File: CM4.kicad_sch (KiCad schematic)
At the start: 11 parts, among them J11 Conn_02x05_Odd_Even, J13 Conn_01x02, J14 Conn_01x02, J15 Conn_01x02, J6 HDMI_A_2.0, U1 RaspberryPi-CM4Lite, U100 DF40C-100DS-0.4V(51), U101 DF40C-100DS-0.4V(51)

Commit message: Adjust Manufacturer/PartNumber for some parts
- Use Diodes B2100-13-F consistently
- Define part for pin headers
- Replace N-Channel MOSFET for PoE with BSZ440N10NS3GATMA1
- Define Input protection MOSFET DMP3013SFV-7

Signed-off-by: Stefan Agner <stefan@agner.ch>
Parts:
- J13, J14, J15: Manufacturer (none) -> Adam Tech; PartNumber (none) -> PH1-02-UA
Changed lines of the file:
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@@
     (comment 2 "Light Blue")
   )
+  (bus_alias "PCIe" (members "~RST" "~CLKREQ" "CLK+" "CLK-" "TX+" "TX-" "RX+" "RX-"))
+  (bus_alias "SD" (members "D[0..3]" "CMD" "CLK" "PWR" "DET"))
+  (bus_alias "HDMI" (members "D0+" "D0-" "D1+" "D1-" "D2+" "D2-" "CLK+" "CLK-" "CEC" "HPD" "SDA" "SCL"))
   (bus_alias "UART" (members "TXD" "RXD" "CTS" "RTS"))
-  (bus_alias "HDMI" (members "D0+" "D0-" "D1+" "D1-" "D2+" "D2-" "CLK+" "CLK-" "CEC" "HPD" "SDA" "SCL"))
-  (bus_alias "SD" (members "D[0..3]" "CMD" "CLK" "PWR" "DET"))
-  (bus_alias "PCIe" (members "~RST" "~CLKREQ" "CLK+" "CLK-" "TX+" "TX-" "RX+" "RX-"))
   (junction (at 59.055 173.99) (diameter 0.9144) (color 0 0 0 0))
   (junction (at 121.92 171.45) (diameter 0.9144) (color 0 0 0 0))
@@
       (effects (font (size 1.27 1.27)) hide)
     )
+    (property "Manufacturer" "Adam Tech" (id 4) (at 133.985 157.48 0)
+      (effects (font (size 1.27 1.27)) hide)
+    )
+    (property "PartNumber" "PH1-02-UA" (id 5) (at 133.985 157.48 0)
+      (effects (font (size 1.27 1.27)) hide)
+    )
     (pin "1")
     (pin "2")
@@
     )
     (property "Config" "DNP" (id 4) (at 139.065 174.625 0))
+    (property "Manufacturer" "Adam Tech" (id 5) (at 133.985 171.45 0)
+      (effects (font (size 1.27 1.27)) hide)
+    )
+    (property "PartNumber" "PH1-02-UA" (id 6) (at 133.985 171.45 0)
+      (effects (font (size 1.27 1.27)) hide)
+    )
     (pin "1")
     (pin "2")
@@
     )
     (property "Config" "DNP" (id 4) (at 139.065 186.69 0))
+    (property "Manufacturer" "Adam Tech" (id 5) (at 133.985 182.88 0)
+      (effects (font (size 1.27 1.27)) hide)
+    )
+    (property "PartNumber" "PH1-02-UA" (id 6) (at 133.985 182.88 0)
+      (effects (font (size 1.27 1.27)) hide)
+    )
     (pin "1")
     (pin "2")

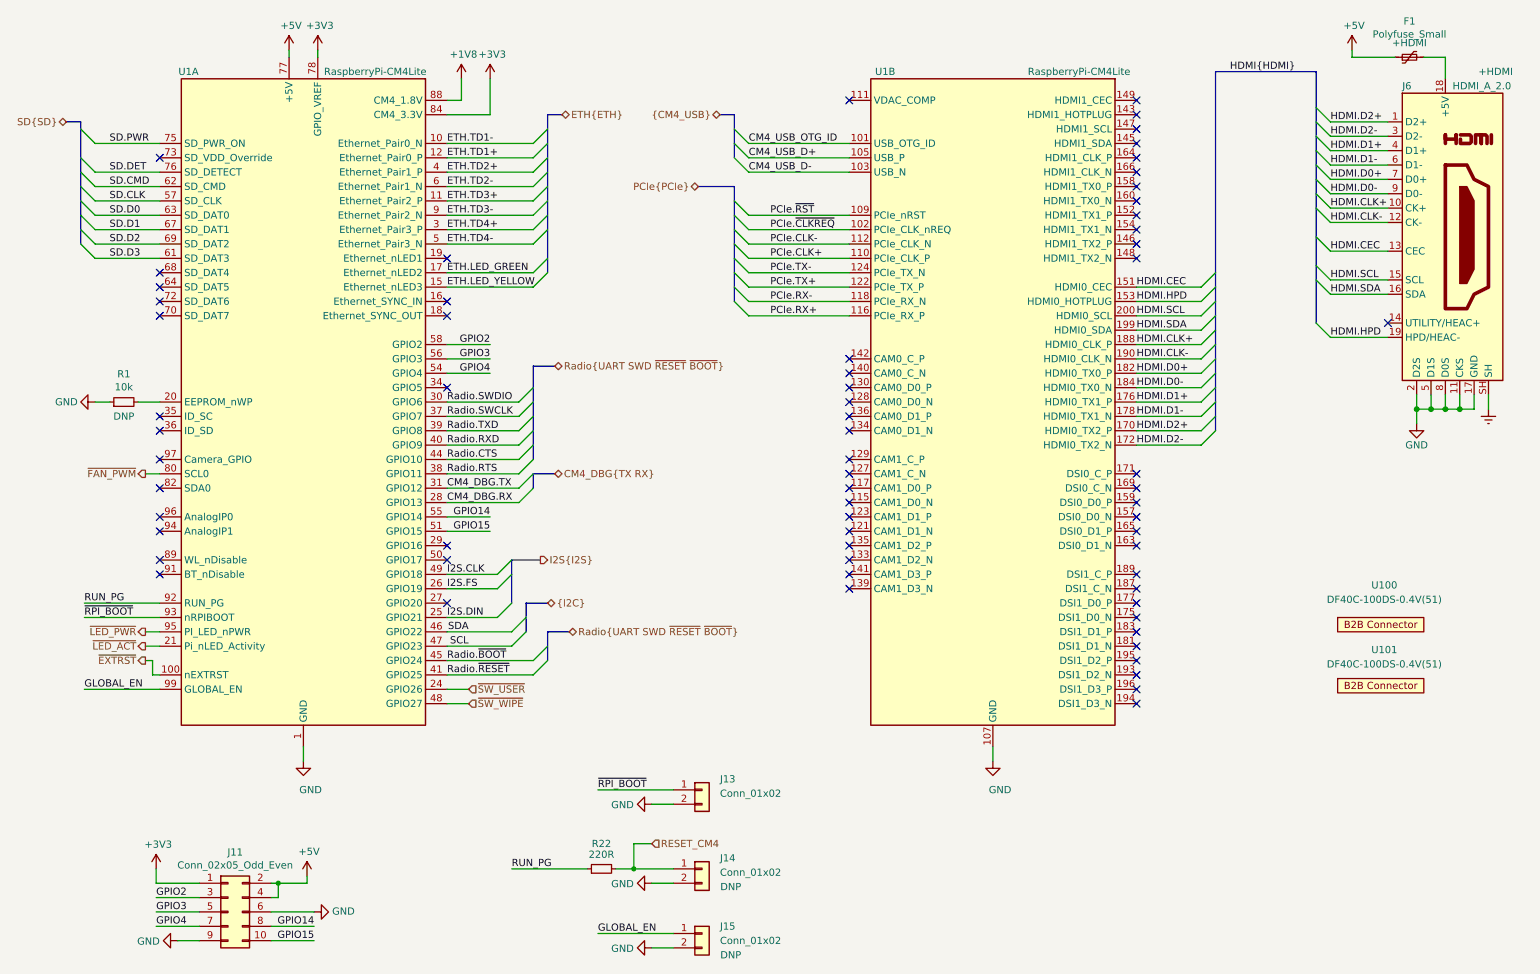
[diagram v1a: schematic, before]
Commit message: Reannotate the complete schematics
Signed-off-by: Stefan Agner <stefan@agner.ch>
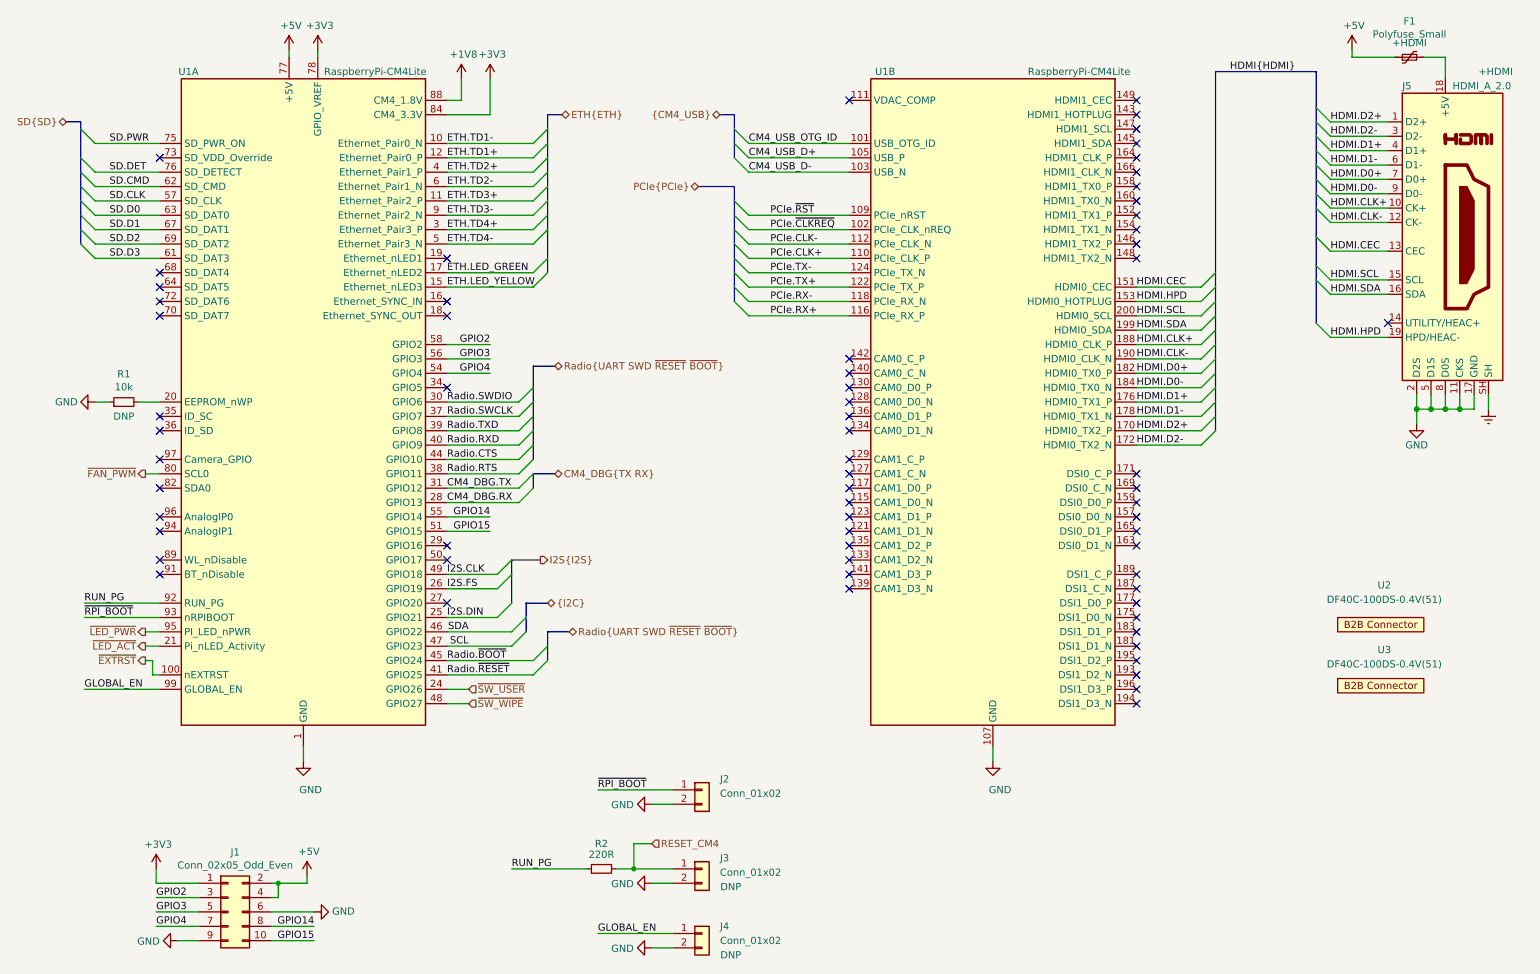
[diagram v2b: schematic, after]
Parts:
- renumbered J11 to J1, J13 to J2, J14 to J3, J15 to J4, J6 to J5, R22 to R2, U100 to U2, U101 to U3
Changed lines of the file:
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@@
   (symbol (lib_id "power:+3V3") (at 37.465 171.45 0) (unit 1)
     (in_bom yes) (on_board yes)
-    (property "Reference" "#PWR0111" (id 0) (at 37.465 175.26 0)
+    (property "Reference" "#PWR02" (id 0) (at 37.465 175.26 0)
       (effects (font (size 1.27 1.27)) hide)
     )
@@
   (symbol (lib_id "power:+5V") (at 60.96 26.67 0) (unit 1)
     (in_bom yes) (on_board yes)
-    (property "Reference" "#PWR0105" (id 0) (at 60.96 30.48 0)
+    (property "Reference" "#PWR04" (id 0) (at 60.96 30.48 0)
       (effects (font (size 1.27 1.27)) hide)
     )
@@
   (symbol (lib_id "power:+5V") (at 64.135 172.72 0) (unit 1)
     (in_bom yes) (on_board yes)
-    (property "Reference" "#PWR0112" (id 0) (at 64.135 176.53 0)
+    (property "Reference" "#PWR06" (id 0) (at 64.135 176.53 0)
       (effects (font (size 1.27 1.27)) hide)
     )
@@
   (symbol (lib_id "power:+3V3") (at 66.04 26.67 0) (unit 1)
     (in_bom yes) (on_board yes)
-    (property "Reference" "#PWR0106" (id 0) (at 66.04 30.48 0)
+    (property "Reference" "#PWR08" (id 0) (at 66.04 30.48 0)
       (effects (font (size 1.27 1.27)) hide)
     )
@@
   (symbol (lib_id "power:+1V8") (at 91.44 31.75 0) (unit 1)
     (in_bom yes) (on_board yes)
-    (property "Reference" "#PWR0107" (id 0) (at 91.44 35.56 0)
+    (property "Reference" "#PWR09" (id 0) (at 91.44 35.56 0)
       (effects (font (size 1.27 1.27)) hide)
     )
@@
   (symbol (lib_id "power:+3V3") (at 96.52 31.75 0) (unit 1)
     (in_bom yes) (on_board yes)
-    (property "Reference" "#PWR0108" (id 0) (at 96.52 35.56 0)
+    (property "Reference" "#PWR010" (id 0) (at 96.52 35.56 0)
       (effects (font (size 1.27 1.27)) hide)
     )
@@
   (symbol (lib_id "power:+5V") (at 248.92 26.67 0) (unit 1)
     (in_bom yes) (on_board yes)
-    (property "Reference" "#PWR0103" (id 0) (at 248.92 30.48 0)
+    (property "Reference" "#PWR015" (id 0) (at 248.92 30.48 0)
       (effects (font (size 1.27 1.27)) hide)
     )
@@
   (symbol (lib_id "power:GND") (at 26.67 88.9 270) (unit 1)
     (in_bom yes) (on_board yes)
-    (property "Reference" "#PWR0104" (id 0) (at 20.32 88.9 0)
+    (property "Reference" "#PWR01" (id 0) (at 20.32 88.9 0)
       (effects (font (size 1.27 1.27)) hide)
     )
@@
   (symbol (lib_id "power:GND") (at 41.275 184.15 270) (unit 1)
     (in_bom yes) (on_board yes)
-    (property "Reference" "#PWR0110" (id 0) (at 34.925 184.15 0)
+    (property "Reference" "#PWR03" (id 0) (at 34.925 184.15 0)
       (effects (font (size 1.27 1.27)) hide)
     )
@@
   (symbol (lib_id "power:GND") (at 63.5 152.4 0) (unit 1)
     (in_bom yes) (on_board yes)
-    (property "Reference" "#PWR0109" (id 0) (at 63.5 158.75 0)
+    (property "Reference" "#PWR05" (id 0) (at 63.5 158.75 0)
       (effects (font (size 1.27 1.27)) hide)
     )
@@
   (symbol (lib_id "power:GND") (at 65.405 179.07 90) (unit 1)
     (in_bom yes) (on_board yes)
-    (property "Reference" "#PWR0113" (id 0) (at 71.755 179.07 0)
+    (property "Reference" "#PWR07" (id 0) (at 71.755 179.07 0)
       (effects (font (size 1.27 1.27)) hide)
     )
@@
   (symbol (lib_id "power:GND") (at 125.095 160.02 270) (unit 1)
     (in_bom yes) (on_board yes)
-    (property "Reference" "#PWR0190" (id 0) (at 118.745 160.02 0)
+    (property "Reference" "#PWR011" (id 0) (at 118.745 160.02 0)
       (effects (font (size 1.27 1.27)) hide)
     )
@@
   (symbol (lib_id "power:GND") (at 125.095 173.99 270) (unit 1)
     (in_bom yes) (on_board yes)
-    (property "Reference" "#PWR0127" (id 0) (at 118.745 173.99 0)
+    (property "Reference" "#PWR012" (id 0) (at 118.745 173.99 0)
       (effects (font (size 1.27 1.27)) hide)
     )
@@
   (symbol (lib_id "power:GND") (at 125.095 185.42 270) (unit 1)
     (in_bom yes) (on_board yes)
-    (property "Reference" "#PWR0125" (id 0) (at 118.745 185.42 0)
+    (property "Reference" "#PWR013" (id 0) (at 118.745 185.42 0)
       (effects (font (size 1.27 1.27)) hide)
     )
@@
   (symbol (lib_id "power:GND") (at 185.42 152.4 0) (unit 1)
     (in_bom yes) (on_board yes)
-    (property "Reference" "#PWR0114" (id 0) (at 185.42 158.75 0)
+    (property "Reference" "#PWR014" (id 0) (at 185.42 158.75 0)
       (effects (font (size 1.27 1.27)) hide)
     )
@@
   (symbol (lib_id "power:GND") (at 260.35 92.71 0) (unit 1)
     (in_bom yes) (on_board yes)
-    (property "Reference" "#PWR0101" (id 0) (at 260.35 99.06 0)
+    (property "Reference" "#PWR016" (id 0) (at 260.35 99.06 0)
       (effects (font (size 1.27 1.27)) hide)
     )
@@
   (symbol (lib_id "power:Earth") (at 273.05 90.17 0) (unit 1)
     (in_bom yes) (on_board yes)
-    (property "Reference" "#PWR0102" (id 0) (at 273.05 96.52 0)
+    (property "Reference" "#PWR017" (id 0) (at 273.05 96.52 0)
       (effects (font (size 1.27 1.27)) hide)
     )
@@
   (symbol (lib_id "Device:R_Small") (at 116.205 171.45 90) (unit 1)
     (in_bom yes) (on_board yes)
-    (property "Reference" "R22" (id 0) (at 116.205 167.005 90))
+    (property "Reference" "R2" (id 0) (at 116.205 167.005 90))
     (property "Value" "220R" (id 1) (at 116.205 168.91 90))
     (property "Footprint" "Resistor_SMD:R_0402_1005Metric" (id 2) (at 116.205 171.45 0)
@@
   (symbol (lib_id "Connector_Generic:Conn_01x02") (at 133.985 157.48 0) (unit 1)
     (in_bom yes) (on_board yes)
-    (property "Reference" "J13" (id 0) (at 137.16 155.5749 0)
+    (property "Reference" "J2" (id 0) (at 137.16 155.5749 0)
       (effects (font (size 1.27 1.27)) (justify left))
     )
@@
   (symbol (lib_id "Connector_Generic:Conn_01x02") (at 133.985 171.45 0) (unit 1)
     (in_bom yes) (on_board yes)
-    (property "Reference" "J14" (id 0) (at 137.16 169.5449 0)
+    (property "Reference" "J3" (id 0) (at 137.16 169.5449 0)
       (effects (font (size 1.27 1.27)) (justify left))
     )
@@
   (symbol (lib_id "Connector_Generic:Conn_01x02") (at 133.985 182.88 0) (unit 1)
     (in_bom yes) (on_board yes)
-    (property "Reference" "J15" (id 0) (at 137.16 181.6099 0)
+    (property "Reference" "J4" (id 0) (at 137.16 181.6099 0)
       (effects (font (size 1.27 1.27)) (justify left))
     )
@@
   (symbol (lib_id "LightBlue:DF40C-100DS-0.4V(51)") (at 254 128.27 0) (unit 1)
     (in_bom yes) (on_board no)
-    (property "Reference" "U100" (id 0) (at 254.635 121.285 0))
+    (property "Reference" "U2" (id 0) (at 254.635 121.285 0))
     (property "Value" "DF40C-100DS-0.4V(51)" (id 1) (at 254.635 123.825 0))
     (property "Footprint" "" (id 2) (at 254 128.27 0)
@@
   (symbol (lib_id "LightBlue:DF40C-100DS-0.4V(51)") (at 254 139.065 0) (unit 1)
     (in_bom yes) (on_board no)
-    (property "Reference" "U101" (id 0) (at 254.635 132.715 0))
+    (property "Reference" "U3" (id 0) (at 254.635 132.715 0))
     (property "Value" "DF40C-100DS-0.4V(51)" (id 1) (at 254.635 135.255 0))
     (property "Footprint" "" (id 2) (at 254 139.065 0)
@@
   (symbol (lib_id "Connector_Generic:Conn_02x05_Odd_Even") (at 50.165 179.07 0) (unit 1)
     (in_bom yes) (on_board yes)
-    (property "Reference" "J11" (id 0) (at 51.435 168.5098 0))
+    (property "Reference" "J1" (id 0) (at 51.435 168.5098 0))
     (property "Value" "Conn_02x05_Odd_Even" (id 1) (at 51.435 170.8085 0))
     (property "Footprint" "Connector_PinHeader_2.54mm:PinHeader_2x05_P2.54mm_Vertical" (id 2) (at 50.165 179.07 0)
@@
   (symbol (lib_id "Connector:HDMI_A_1.4") (at 265.43 59.69 0) (unit 1)
     (in_bom yes) (on_board yes)
-    (property "Reference" "J6" (id 0) (at 257.81 33.02 0)
-      (effects (font (size 1.27 1.27)) (justify left))
-    )
+    (property "Reference" "J5" (id 0) (at 257.81 33.02 0)
+      (effects (font (size 1.27 1.27)) (justify left))
+    )

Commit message: Adjust rating/footprint size of some ceramic capacitors
Also update connector/jumper designator to make more sense.

Signed-off-by: Stefan Agner <stefan@agner.ch>
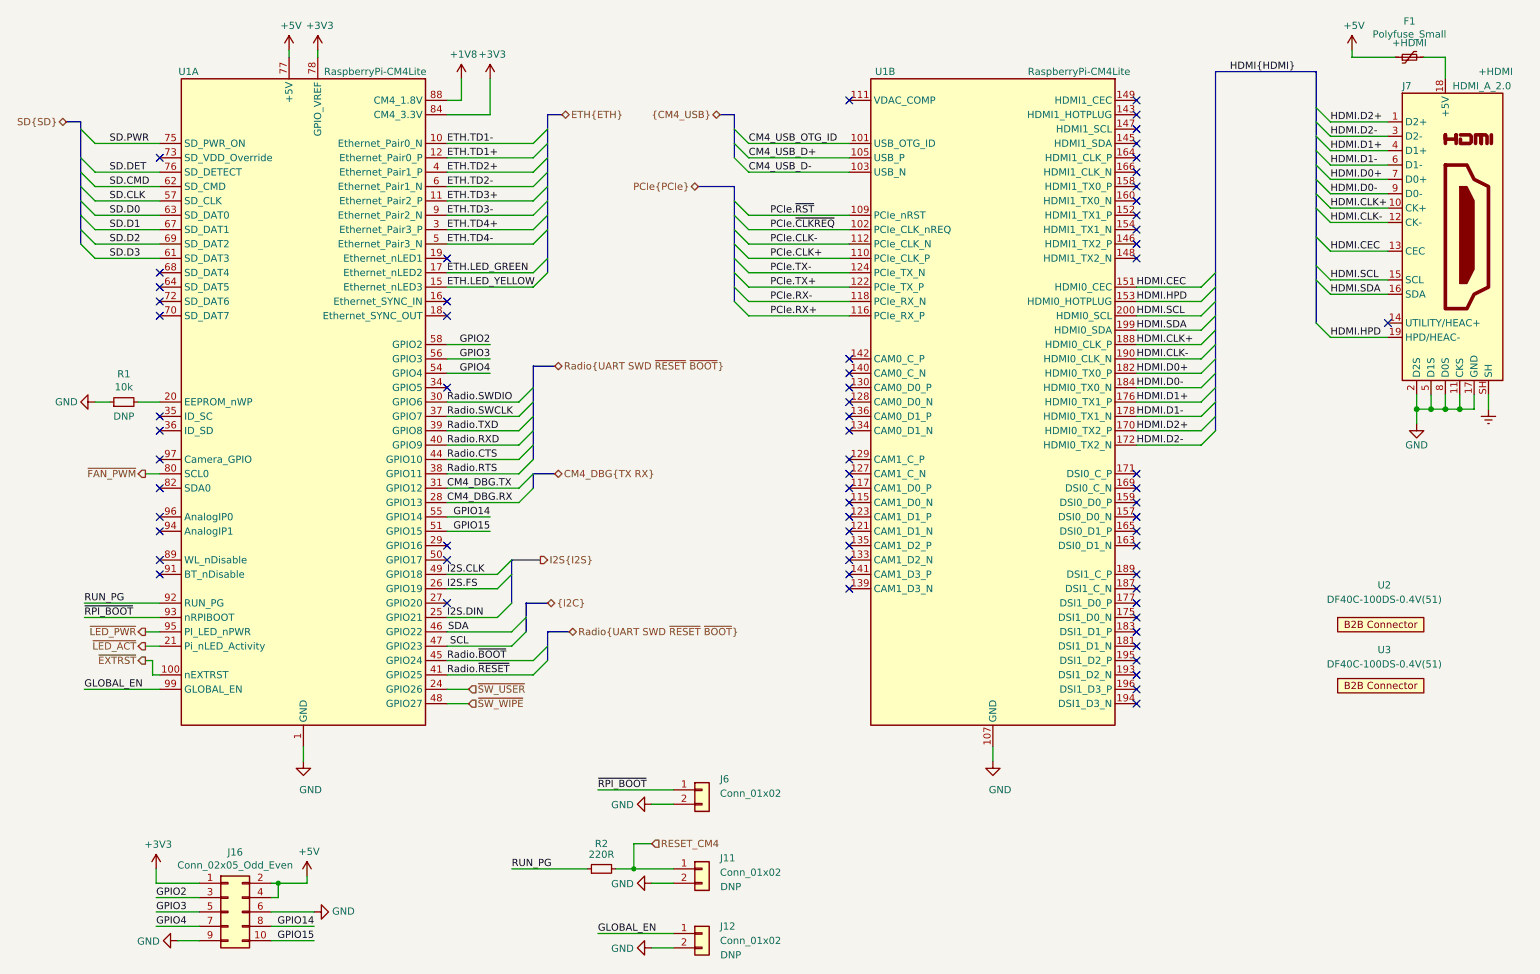
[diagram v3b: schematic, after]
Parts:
- renumbered J3 to J11, J4 to J12, J1 to J16, J2 to J6, J5 to J7
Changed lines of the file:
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@@
   (symbol (lib_id "Connector_Generic:Conn_01x02") (at 133.985 157.48 0) (unit 1)
     (in_bom yes) (on_board yes)
-    (property "Reference" "J2" (id 0) (at 137.16 155.5749 0)
+    (property "Reference" "J6" (id 0) (at 137.16 155.5749 0)
       (effects (font (size 1.27 1.27)) (justify left))
     )
@@
   (symbol (lib_id "Connector_Generic:Conn_01x02") (at 133.985 171.45 0) (unit 1)
     (in_bom yes) (on_board yes)
-    (property "Reference" "J3" (id 0) (at 137.16 169.5449 0)
+    (property "Reference" "J11" (id 0) (at 137.16 169.5449 0)
       (effects (font (size 1.27 1.27)) (justify left))
     )
@@
   (symbol (lib_id "Connector_Generic:Conn_01x02") (at 133.985 182.88 0) (unit 1)
     (in_bom yes) (on_board yes)
-    (property "Reference" "J4" (id 0) (at 137.16 181.6099 0)
+    (property "Reference" "J12" (id 0) (at 137.16 181.6099 0)
       (effects (font (size 1.27 1.27)) (justify left))
     )
@@
   (symbol (lib_id "Connector_Generic:Conn_02x05_Odd_Even") (at 50.165 179.07 0) (unit 1)
     (in_bom yes) (on_board yes)
-    (property "Reference" "J1" (id 0) (at 51.435 168.5098 0))
+    (property "Reference" "J16" (id 0) (at 51.435 168.5098 0))
     (property "Value" "Conn_02x05_Odd_Even" (id 1) (at 51.435 170.8085 0))
     (property "Footprint" "Connector_PinHeader_2.54mm:PinHeader_2x05_P2.54mm_Vertical" (id 2) (at 50.165 179.07 0)
@@
   (symbol (lib_id "Connector:HDMI_A_1.4") (at 265.43 59.69 0) (unit 1)
     (in_bom yes) (on_board yes)
-    (property "Reference" "J5" (id 0) (at 257.81 33.02 0)
+    (property "Reference" "J7" (id 0) (at 257.81 33.02 0)
       (effects (font (size 1.27 1.27)) (justify left))
     )
